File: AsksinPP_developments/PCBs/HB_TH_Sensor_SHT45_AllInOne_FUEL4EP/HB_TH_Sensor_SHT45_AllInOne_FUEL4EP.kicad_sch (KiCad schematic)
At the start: 41 parts, among them J1 Conn_01x03, J2 FTDI Debuger, J3 ISP Programmer, SW1 Config button, U1 ATmega1284P-AU, U2 TPS61221DCK, U3 SHT45-AD1F-R2

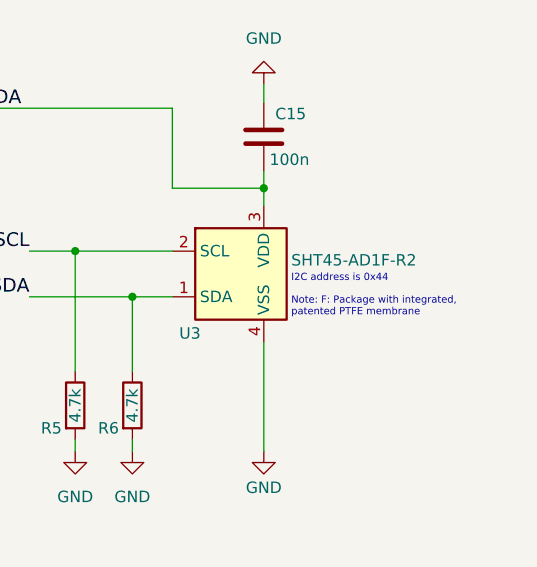
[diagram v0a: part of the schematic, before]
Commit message: PCBs: HB_TH_Sensor_SHT45_AllInOne_FUEL4EP and I2C_Module_SHT45_BME280_FUEL4EP: replacement of SHT45 to type without PTFE filter
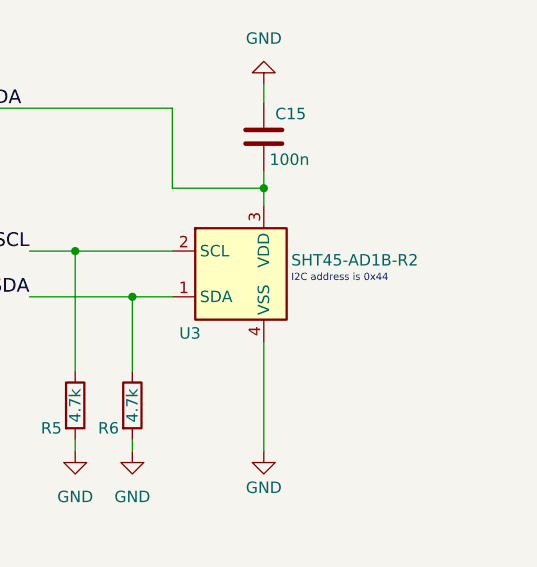
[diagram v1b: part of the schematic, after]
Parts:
- U3: value SHT45-AD1F-R2 -> SHT45-AD1B-R2; LCSC C5360602 -> C5221601
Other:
- note removed: "Note: F: Package with integrated, patented PTFE membrane"
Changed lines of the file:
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@@
     (title "HB_TH_Sensor_SHT45_AllInOne_FUEL4EP")
     (date "2023-12-15")
-    (rev "1.0")
+    (rev "1.1")
     (company "(C) FUEL4EP")
     (comment 1 "Creative Commons License, non-commercial")
@@
   (text "1x Keystone 2460\nbattery holder" (at 45.72 31.75 0)
     (effects (font (size 1.524 1.524)) (justify left bottom))
-  )
-  (text "Note: F: Package with integrated,\npatented PTFE membrane"
-    (at 257.048 50.546 0)
-    (effects (font (size 0.8 0.8)) (justify left bottom))
   )
   (label "SCL" (at 88.265 137.16 180)
@@
       (effects (font (size 1.27 1.27)) (justify left))
     )
-    (property "Value" "SHT45-AD1F-R2" (id 1) (at 257.048 44.196 0)
+    (property "Value" "SHT45-AD1B-R2" (id 1) (at 257.048 44.196 0)
       (effects (font (size 1.27 1.27)) (justify left))
     )
@@
       (effects (font (size 1.27 1.27)) (justify left) hide)
     )
-    (property "LCSC" "C5360602" (id 4) (at 251.46 45.72 0)
+    (property "LCSC" "C5221601" (id 4) (at 251.46 45.72 0)
       (effects (font (size 1.524 1.524)) hide)
     )
@@
     )
     (path "/bc06256e-795c-431e-82f4-646a591b6737"
-      (reference "U3") (unit 1) (value "SHT45-AD1F-R2") (footprint "FUEL4EP:SHT4X")
-    )
-  )
+      (reference "U3") (unit 1) (value "SHT45-AD1B-R2") (footprint "FUEL4EP:SHT4X")
+    )
+  )

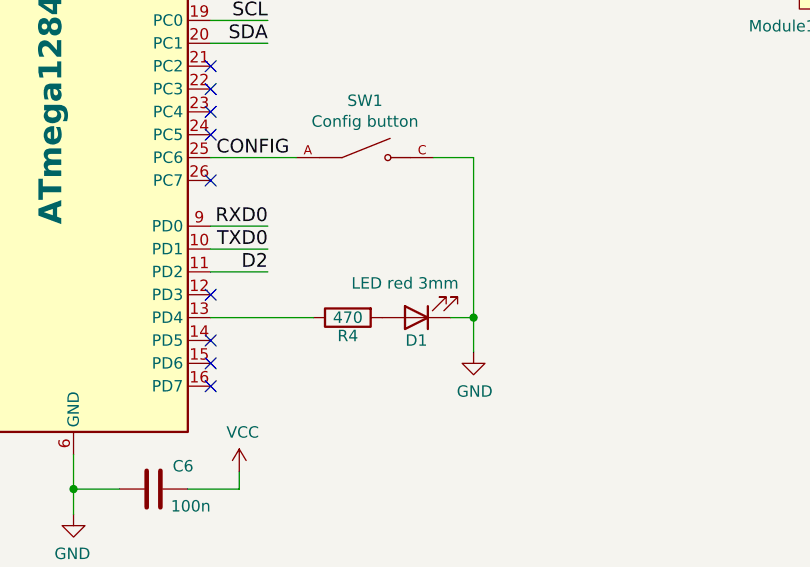
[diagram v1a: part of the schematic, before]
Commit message: PCBs: HB_TH_Sensor_SHT45_AllInOne_FUEL4EP and HB-UNI-SEN-BATT_ATMega1284P_E07-900MM10S_FUEL4EP: fix of wrong LCSC part numbers
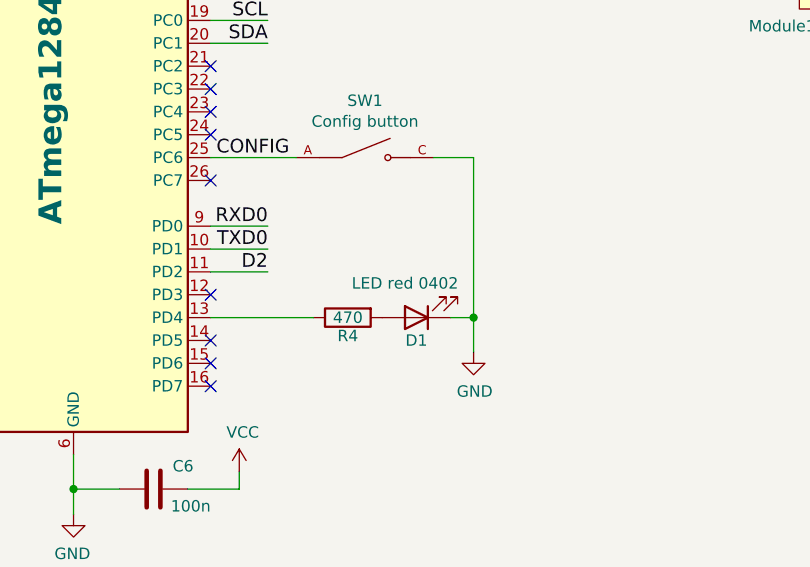
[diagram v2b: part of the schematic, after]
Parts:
- D1: value LED red 3mm -> LED red 0402; LCSC C84256 -> C273598; TYPE LED_0805 -> 0402
- R1: LCSC C17733 -> C25744; TYPE 0805 -> 0402
- R4: LCSC C17710 -> C25117; TYPE 0805 -> 0402
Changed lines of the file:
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@@
   (title_block
     (title "HB_TH_Sensor_SHT45_AllInOne_FUEL4EP")
-    (date "2023-12-15")
-    (rev "1.1")
+    (date "2024-01-08")
+    (rev "1.2")
     (company "(C) FUEL4EP")
     (comment 1 "Creative Commons License, non-commercial")
@@
     (in_bom yes) (on_board yes)
     (property "Reference" "D1" (id 0) (at 104.775 172.72 0))
-    (property "Value" "LED red 3mm" (id 1) (at 103.505 166.37 0))
+    (property "Value" "LED red 0402" (id 1) (at 103.505 166.37 0))
     (property "Footprint" "LED_SMD:LED_0402_1005Metric" (id 2) (at 104.775 170.18 0)
       (effects (font (size 1.27 1.27)) hide)
     )
-    (property "Datasheet" "https://datasheet.lcsc.com/lcsc/2008201032_Foshan-NationStar-Optoelectronics-NCD0805R1_C84256.pdf" (id 3) (at 104.775 170.18 0)
-      (effects (font (size 1.27 1.27)) hide)
-    )
-    (property "TYPE" "LED_0805" (id 4) (at 104.775 170.18 0)
-      (effects (font (size 1.27 1.27)) hide)
-    )
-    (property "LCSC" "C84256" (id 5) (at 104.775 170.18 0)
+    (property "Datasheet" "https://datasheet.lcsc.com/lcsc/1810191241_TOGIALED-TJ-S1005SW4TGLC2R-A5_C273598.pdf" (id 3) (at 104.775 170.18 0)
+      (effects (font (size 1.27 1.27)) hide)
+    )
+    (property "TYPE" "0402" (id 4) (at 104.775 170.18 0)
+      (effects (font (size 1.27 1.27)) hide)
+    )
+    (property "LCSC" "C273598" (id 5) (at 104.775 170.18 0)
       (effects (font (size 1.27 1.27)) hide)
     )
@@
       (effects (font (size 1.27 1.27)) hide)
     )
-    (property "Datasheet" "https://datasheet.lcsc.com/lcsc/1811050105_UNI-ROYAL-Uniroyal-Elec-0805W8F4700T5E_C17710.pdf" (id 3) (at 97.155 170.18 0)
-      (effects (font (size 1.27 1.27)) hide)
-    )
-    (property "TYPE" "0805" (id 4) (at 97.155 170.18 0)
-      (effects (font (size 1.27 1.27)) hide)
-    )
-    (property "LCSC" "C17710" (id 5) (at 97.155 170.18 0)
+    (property "Datasheet" "https://datasheet.lcsc.com/lcsc/2205311900_UNI-ROYAL-Uniroyal-Elec-0402WGF4700TCE_C25117.pdf" (id 3) (at 97.155 170.18 0)
+      (effects (font (size 1.27 1.27)) hide)
+    )
+    (property "TYPE" "0402" (id 4) (at 97.155 170.18 0)
+      (effects (font (size 1.27 1.27)) hide)
+    )
+    (property "LCSC" "C25117" (id 5) (at 97.155 170.18 0)
       (effects (font (size 1.27 1.27)) hide)
     )
@@
       (effects (font (size 1.27 1.27)) hide)
     )
-    (property "Datasheet" "https://datasheet.lcsc.com/lcsc/1810301817_UNI-ROYAL-Uniroyal-Elec-0805W8F5103T5E_C17733.pdf" (id 3) (at 45.085 67.31 0)
-      (effects (font (size 1.27 1.27)) hide)
-    )
-    (property "TYPE" "0805" (id 4) (at 45.085 67.31 0)
-      (effects (font (size 1.27 1.27)) hide)
-    )
-    (property "LCSC" "C17733" (id 5) (at 45.085 67.31 0)
+    (property "Datasheet" "https://datasheet.lcsc.com/lcsc/2206010100_UNI-ROYAL-Uniroyal-Elec-0402WGF1002TCE_C25744.pdf" (id 3) (at 45.085 67.31 0)
+      (effects (font (size 1.27 1.27)) hide)
+    )
+    (property "TYPE" "0402" (id 4) (at 45.085 67.31 0)
+      (effects (font (size 1.27 1.27)) hide)
+    )
+    (property "LCSC" "C25744" (id 5) (at 45.085 67.31 0)
       (effects (font (size 1.27 1.27)) hide)
     )
@@
     )
     (path "/00000000-0000-0000-0000-00005abe1195"
-      (reference "D1") (unit 1) (value "LED red 3mm") (footprint "LED_SMD:LED_0402_1005Metric")
+      (reference "D1") (unit 1) (value "LED red 0402") (footprint "LED_SMD:LED_0402_1005Metric")
     )
     (path "/cbee9fdc-0bb0-41ab-be9a-430283873214"

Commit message: PCBs: HB_TH_Sensor_SHT45_AllInOne_FUEL4EP (updates), added HB_Stamp_ATMega1284P_FUEL4EP and I2C_Module_SHT45_BME280_small_FUEL4EP
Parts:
- U2: LCSC C37055 -> C2865756
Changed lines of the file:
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@@
   (title_block
     (title "HB_TH_Sensor_SHT45_AllInOne_FUEL4EP")
-    (date "2024-01-08")
-    (rev "1.2")
+    (date "2024-01-13")
+    (rev "1.3")
     (company "(C) FUEL4EP")
     (comment 1 "Creative Commons License, non-commercial")
@@
       (effects (font (size 1.27 1.27)) hide)
     )
-    (property "LCSC" "C37055" (id 4) (at 114.935 33.655 0)
-      (effects (font (size 1.27 1.27)) hide)
-    )
+    (property "LCSC" "C2865756" (id 4) (at 114.935 33.655 0)
+      (effects (font (size 1.27 1.27)) hide)
+    )

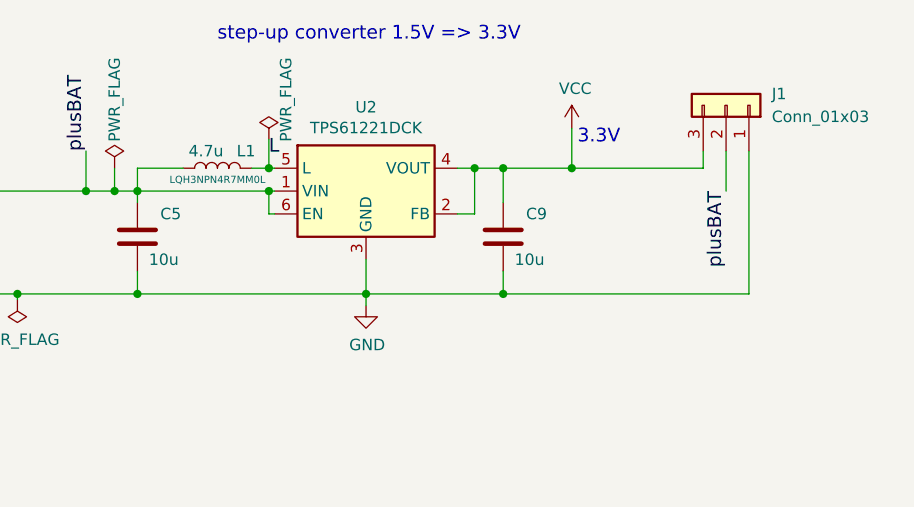
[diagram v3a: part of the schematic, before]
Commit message: PCBs: updates of HB_TH_Sensor_SHT45_AllInOne_FUEL4EP and HB_Stamp_ATMega1284P_FUEL4EP see README.mds
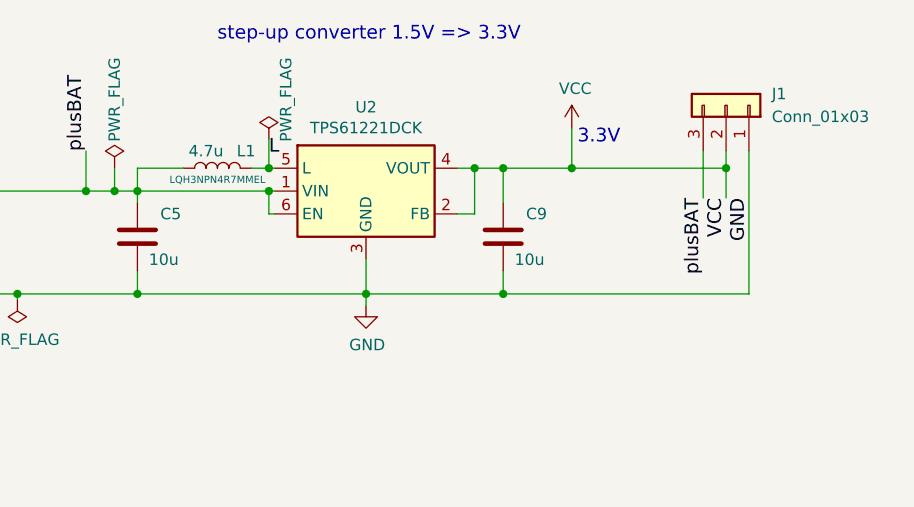
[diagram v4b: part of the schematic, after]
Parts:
- L1: LCSC C86077 -> C576538; Productname LQH3NPN4R7MM0L -> LQH3NPN4R7MMEL; TYPE 0 -> 1212
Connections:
- net VCC: now also J1.2 (Pin_2); no longer J1.3 (Pin_3)
- net plusBAT: now also J1.3 (Pin_3); no longer J1.2 (Pin_2)
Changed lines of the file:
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@@
   (title_block
     (title "HB_TH_Sensor_SHT45_AllInOne_FUEL4EP")
-    (date "2024-01-13")
-    (rev "1.3")
+    (date "2024-01-21")
+    (rev "1.4")
     (company "(C) FUEL4EP")
     (comment 1 "Creative Commons License, non-commercial")
@@
   (junction (at 130.175 31.115) (diameter 0) (color 0 0 0 0)
   )
+  (junction (at 55.245 77.47) (diameter 0) (color 0 0 0 0)
+  )
+  (junction (at 254 36.195) (diameter 0) (color 0 0 0 0)
+  )
+  (junction (at 76.835 80.645) (diameter 0) (color 0 0 0 0)
+  )
+  (junction (at 104.14 33.655) (diameter 0) (color 0 0 0 0)
+  )
   (junction (at 130.175 45.085) (diameter 0) (color 0 0 0 0)
   )
-  (junction (at 55.245 77.47) (diameter 0) (color 0 0 0 0)
-  )
-  (junction (at 254 36.195) (diameter 0) (color 0 0 0 0)
-  )
-  (junction (at 76.835 80.645) (diameter 0) (color 0 0 0 0)
-  )
-  (junction (at 104.14 33.655) (diameter 0) (color 0 0 0 0)
-  )
   (junction (at 89.535 45.085) (diameter 0) (color 0 0 0 0)
   )
@@
   )
   (junction (at 83.82 33.655) (diameter 0) (color 0 0 0 0)
+  )
+  (junction (at 154.94 31.115) (diameter 0) (color 0 0 0 0)
   )
   (junction (at 217.17 27.305) (diameter 0) (color 0 0 0 0)
@@
     (stroke (width 0) (type default) (color 0 0 0 0))
   )
+  (wire (pts (xy 130.175 45.085) (xy 157.48 45.085))
+    (stroke (width 0) (type default) (color 0 0 0 0))
+  )
   (wire (pts (xy 38.735 110.49) (xy 46.355 110.49))
     (stroke (width 0) (type default) (color 0 0 0 0))
@@
     (stroke (width 0) (type default) (color 0 0 0 0))
   )
-  (wire (pts (xy 130.175 45.085) (xy 157.48 45.085))
-    (stroke (width 0) (type default) (color 0 0 0 0))
-  )
   (wire (pts (xy 80.645 80.645) (xy 76.835 80.645))
     (stroke (width 0) (type default) (color 0 0 0 0))
@@
     (stroke (width 0) (type default) (color 0 0 0 0))
   )
-  (wire (pts (xy 152.4 29.21) (xy 152.4 31.115))
-    (stroke (width 0) (type default) (color 0 0 0 0))
-  )
   (wire (pts (xy 132.08 105.41) (xy 132.08 107.95))
     (stroke (width 0) (type default) (color 0 0 0 0))
@@
     (stroke (width 0) (type default) (color 0 0 0 0))
   )
-  (wire (pts (xy 154.94 29.21) (xy 154.94 33.655))
-    (stroke (width 0) (type default) (color 0 0 0 0))
-  )
   (wire (pts (xy 194.945 27.305) (xy 200.66 27.305))
     (stroke (width 0) (type default) (color 0 0 0 0))
@@
     (stroke (width 0) (type default) (color 0 0 0 0))
   )
-  (wire (pts (xy 137.795 31.115) (xy 152.4 31.115))
+  (wire (pts (xy 137.795 31.115) (xy 154.94 31.115))
     (stroke (width 0) (type default) (color 0 0 0 0))
   )
@@
     (stroke (width 0) (type default) (color 0 0 0 0))
   )
+  (wire (pts (xy 154.94 31.115) (xy 154.94 34.417))
+    (stroke (width 0) (type default) (color 0 0 0 0))
+  )
   (wire (pts (xy 55.245 67.945) (xy 55.245 68.58))
     (stroke (width 0) (type default) (color 0 0 0 0))
@@
     (stroke (width 0) (type default) (color 0 0 0 0))
   )
+  (wire (pts (xy 152.4 29.21) (xy 152.4 34.417))
+    (stroke (width 0) (type default) (color 0 0 0 0))
+  )
   (wire (pts (xy 233.68 102.87) (xy 256.54 102.87))
     (stroke (width 0) (type default) (color 0 0 0 0))
@@
     (stroke (width 0) (type default) (color 0 0 0 0))
   )
+  (wire (pts (xy 154.94 29.21) (xy 154.94 31.115))
+    (stroke (width 0) (type default) (color 0 0 0 0))
+  )
   (wire (pts (xy 233.68 100.33) (xy 233.68 102.87))
     (stroke (width 0) (type default) (color 0 0 0 0))
   )
-  (wire (pts (xy 157.48 29.21) (xy 157.48 45.085))
-    (stroke (width 0) (type default) (color 0 0 0 0))
-  )
   (wire (pts (xy 29.845 91.44) (xy 31.75 91.44))
     (stroke (width 0) (type default) (color 0 0 0 0))
@@
   )
   (wire (pts (xy 69.215 78.105) (xy 69.215 80.645))
+    (stroke (width 0) (type default) (color 0 0 0 0))
+  )
+  (wire (pts (xy 157.48 45.085) (xy 157.48 29.21))
     (stroke (width 0) (type default) (color 0 0 0 0))
   )
@@
     (effects (font (size 1.524 1.524)) (justify right bottom))
   )
+  (label "VCC" (at 154.94 34.417 270)
+    (effects (font (size 1.524 1.524)) (justify right bottom))
+  )
   (label "RSETB" (at 45.085 88.9 0)
     (effects (font (size 1.524 1.524)) (justify left bottom))
@@
     (effects (font (size 1.524 1.524)) (justify left bottom))
   )
-  (label "plusBAT" (at 154.94 33.655 270)
+  (label "plusBAT" (at 152.4 34.417 270)
     (effects (font (size 1.524 1.524)) (justify right bottom))
   )
@@
   (label "RXD0" (at 250.19 95.25 0)
     (effects (font (size 1.524 1.524)) (justify left bottom))
+  )
+  (label "GND" (at 157.48 34.417 270)
+    (effects (font (size 1.524 1.524)) (justify right bottom))
   )
   (label "plusBAT" (at 97.155 91.44 0)
@@
       (effects (font (size 1.27 1.27)) hide)
     )
-    (property "Datasheet" "https://datasheet.lcsc.com/lcsc/1810221721_Murata-Electronics-LQH3NPN4R7MM0L_C86077.pdf" (id 3) (at 98.425 31.115 0)
-      (effects (font (size 1.27 1.27)) hide)
-    )
-    (property "TYPE" "0" (id 4) (at 98.425 31.115 0)
-      (effects (font (size 1.27 1.27)) hide)
-    )
-    (property "LCSC" "C86077" (id 5) (at 101.6 29.21 0)
+    (property "Datasheet" "https://datasheet.lcsc.com/lcsc/2304140030_Murata-Electronics-LQH3NPN4R7MMEL_C576538.pdf" (id 3) (at 98.425 31.115 0)
+      (effects (font (size 1.27 1.27)) hide)
+    )
+    (property "TYPE" "1212" (id 4) (at 98.425 31.115 0)
+      (effects (font (size 1.27 1.27)) hide)
+    )
+    (property "LCSC" "C576538" (id 5) (at 101.6 29.21 0)
       (effects (font (size 1.27 1.27)) hide)
     )
@@
       (effects (font (size 1.524 1.524)) hide)
     )
-    (property "Productname" "LQH3NPN4R7MM0L" (id 7) (at 98.425 32.385 90)
+    (property "Productname" "LQH3NPN4R7MMEL" (id 7) (at 98.425 32.385 90)
       (effects (font (size 0.8 0.8)))
     )

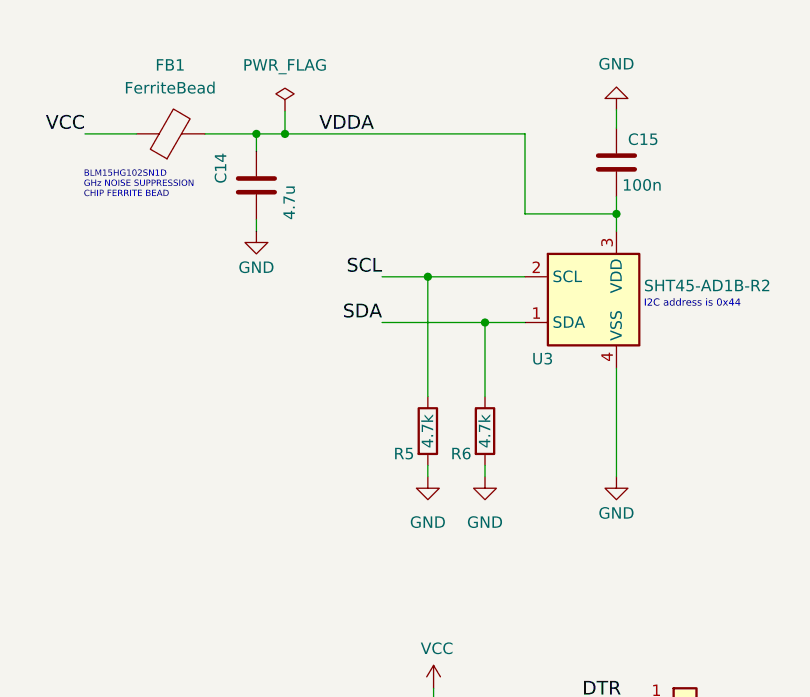
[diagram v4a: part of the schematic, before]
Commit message: PCBs: fix of I2C Pull-up resistors that were wrongly tied to GND
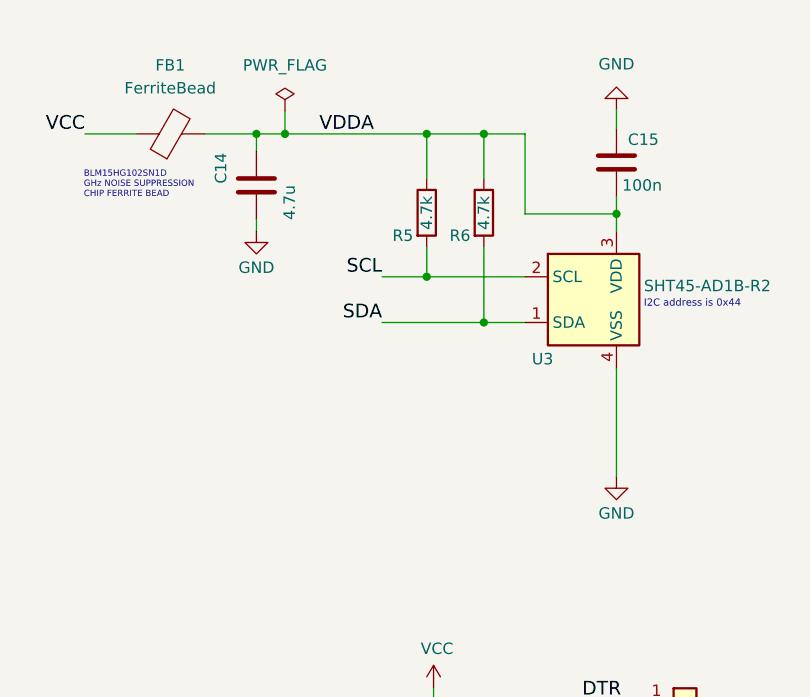
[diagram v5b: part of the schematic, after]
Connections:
- net GND: no longer R5.2, R6.2
- net SCL: now also R5.2; no longer R5.1
- net SDA: now also R6.2; no longer R6.1
- net VDDA: now also R5.1, R6.1
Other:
- moved on the sheet: R5, R6
